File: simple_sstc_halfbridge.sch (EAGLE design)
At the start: 31 parts, among them IC1 IR2153D, J1 DCJ0202, Q1 IRFP240, Q2 IRFP240, Q3 IRLZ44Z

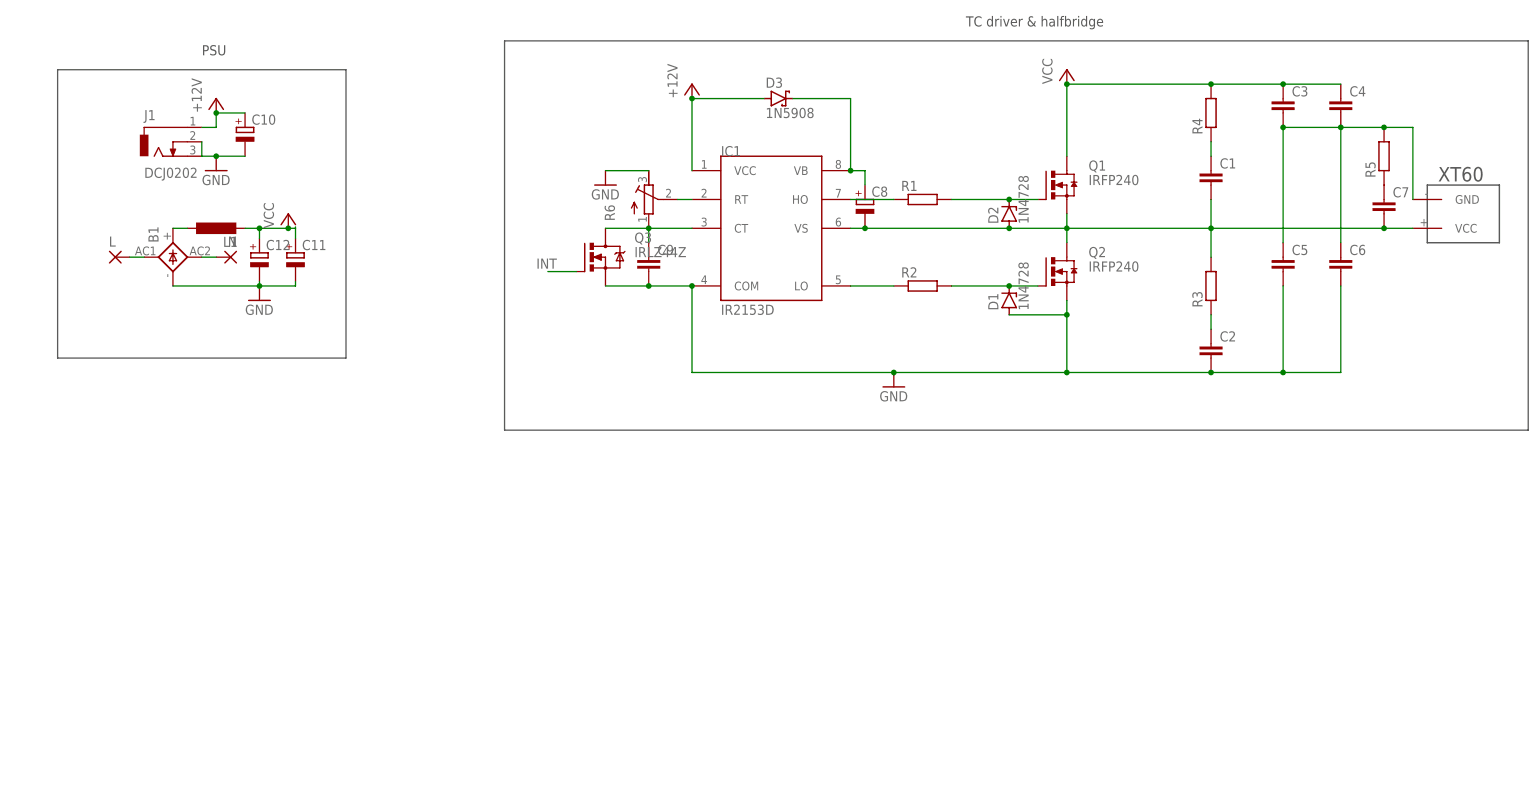
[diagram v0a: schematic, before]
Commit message: Finished driver schematic
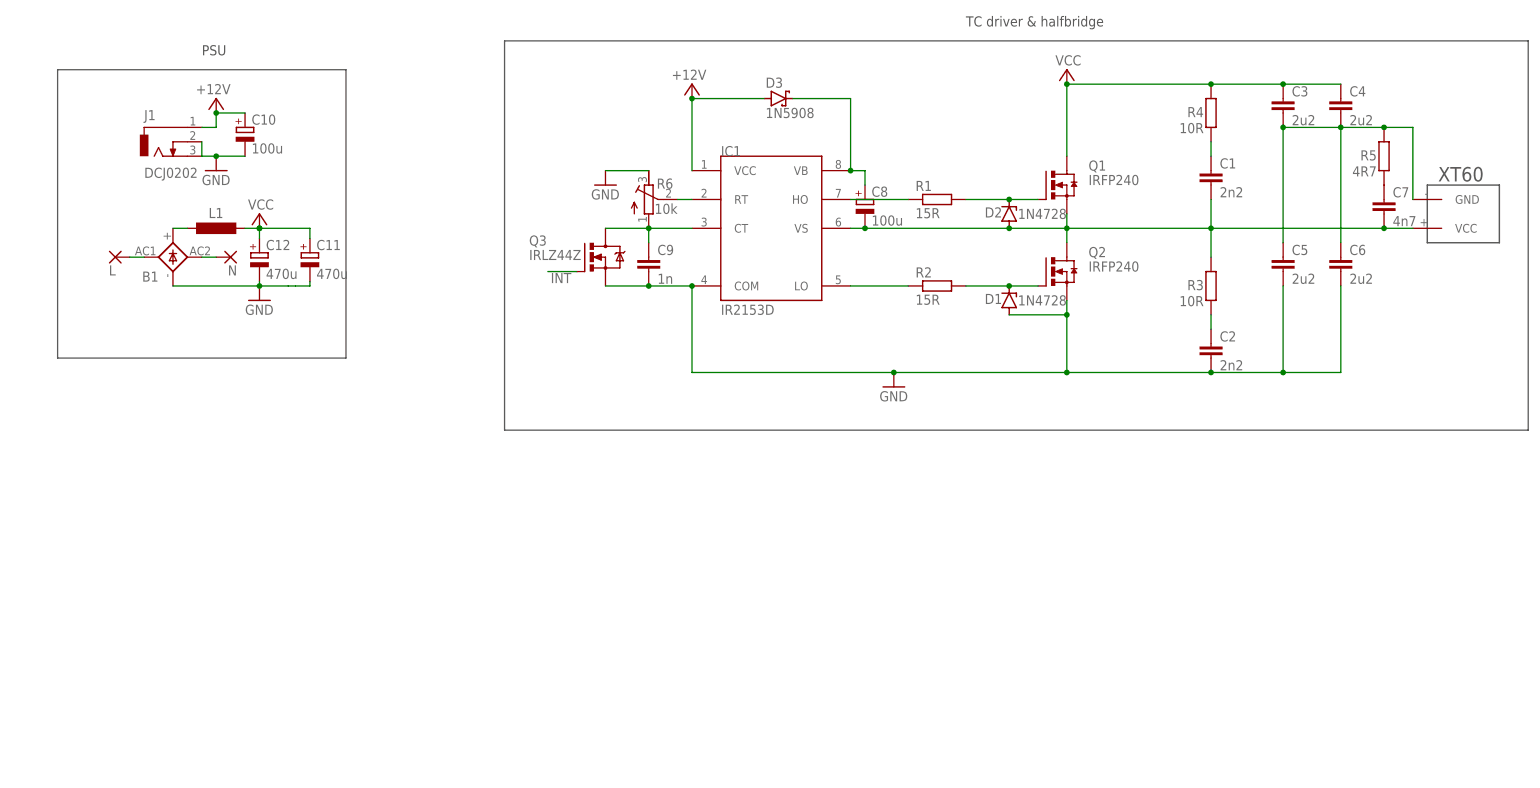
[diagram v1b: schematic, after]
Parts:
- C1, C2: value (none) -> 2n2
- C10, C8: value (none) -> 100u
- C11, C12: value (none) -> 470u
- C3, C4, C5, C6: value (none) -> 2u2
- C7: value (none) -> 4n7
- C9: value (none) -> 1n
- R1, R2: value (none) -> 15R
- R3, R4: value (none) -> 10R
- R5: value (none) -> 4R7
- R6: value (none) -> 10k
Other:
- moved on the sheet: C11, R1, R2

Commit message: Added interrupter
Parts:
- added C13: 10n, rcl:C-EU025-025X050
- added C14: 100n, rcl:C-EU025-025X050
- added IC2: NE555, st-microelectronics:NE555
- added R7: 15k, rcl:R-EU_VMTA55
- added R8: 100k, rcl:R-TRIMM3339P
- added SV1: (no value), con-lstb:MA03-1
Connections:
- new net N$10: IC2.DIS, R7.1, R8.E
- new net N$14: C13.1, IC2.TRE, IC2.TRI, R8.S
- new net N$17: C14.1, IC2.CON
- new net N$19: IC2.OUT, SV1.1
- net GND: now also C13.2, C14.2, IC2.GND, R8.A, SV1.3
- net INT: now also SV1.2
- net VCC: now also IC2./RES, IC2.VCC+, R7.2
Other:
- note added: "Interrupter"
- note added: "Jumper"
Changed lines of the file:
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@@
 <part name="P+3" library="supply1" library_urn="urn:adsk.eagle:library:371" deviceset="VCC" device=""/>
 <part name="P+4" library="supply1" library_urn="urn:adsk.eagle:library:371" deviceset="VCC" device=""/>
+<part name="IC2" library="st-microelectronics" library_urn="urn:adsk.eagle:library:368" deviceset="NE555" device="" package3d_urn="urn:adsk.eagle:package:26829/1"/>
+<part name="C13" library="rcl" library_urn="urn:adsk.eagle:library:334" deviceset="C-EU" device="025-025X050" package3d_urn="urn:adsk.eagle:package:23629/2" value="10n"/>
+<part name="C14" library="rcl" library_urn="urn:adsk.eagle:library:334" deviceset="C-EU" device="025-025X050" package3d_urn="urn:adsk.eagle:package:23629/2" value="100n"/>
+<part name="R7" library="rcl" library_urn="urn:adsk.eagle:library:334" deviceset="R-EU_" device="VMTA55" package3d_urn="urn:adsk.eagle:package:26121/2" value="15k"/>
+<part name="R8" library="rcl" library_urn="urn:adsk.eagle:library:334" deviceset="R-TRIMM" device="3339P" package3d_urn="urn:adsk.eagle:package:23757/1" value="100k"/>
+<part name="P+5" library="supply1" library_urn="urn:adsk.eagle:library:371" deviceset="VCC" device="" value="+12V"/>
+<part name="P+6" library="supply1" library_urn="urn:adsk.eagle:library:371" deviceset="VCC" device="" value="+12V"/>
+<part name="GND5" library="supply1" library_urn="urn:adsk.eagle:library:371" deviceset="GND" device=""/>
+<part name="GND6" library="supply1" library_urn="urn:adsk.eagle:library:371" deviceset="GND" device=""/>
+<part name="SV1" library="con-lstb" library_urn="urn:adsk.eagle:library:162" deviceset="MA03-1" device="" package3d_urn="urn:adsk.eagle:package:8339/1"/>
+<part name="GND7" library="supply1" library_urn="urn:adsk.eagle:library:371" deviceset="GND" device=""/>
+<part name="GND8" library="supply1" library_urn="urn:adsk.eagle:library:371" deviceset="GND" device=""/>
 </parts>
 <sheets>
 <sheet>
 <plain>
-<wire x1="12.7" y1="63.5" x2="63.5" y2="63.5" width="0.1524" layer="97"/>
-<wire x1="63.5" y1="63.5" x2="63.5" y2="12.7" width="0.1524" layer="97"/>
-<wire x1="63.5" y1="12.7" x2="12.7" y2="12.7" width="0.1524" layer="97"/>
-<wire x1="12.7" y1="12.7" x2="12.7" y2="63.5" width="0.1524" layer="97"/>
+<wire x1="12.7" y1="63.5" x2="71.12" y2="63.5" width="0.1524" layer="97"/>
+<wire x1="71.12" y1="63.5" x2="71.12" y2="2.54" width="0.1524" layer="97"/>
+<wire x1="71.12" y1="2.54" x2="12.7" y2="2.54" width="0.1524" layer="97"/>
+<wire x1="12.7" y1="2.54" x2="12.7" y2="63.5" width="0.1524" layer="97"/>
 <wire x1="271.78" y1="68.58" x2="91.44" y2="68.58" width="0.1524" layer="97"/>
 <wire x1="91.44" y1="68.58" x2="91.44" y2="0" width="0.1524" layer="97"/>
@@
 <text x="38.1" y="66.04" size="1.778" layer="97">PSU</text>
 <text x="172.72" y="71.12" size="1.778" layer="97">TC driver &amp; halfbridge</text>
+<wire x1="5.08" y1="-5.08" x2="81.28" y2="-5.08" width="0.1524" layer="97"/>
+<wire x1="81.28" y1="-5.08" x2="81.28" y2="-60.96" width="0.1524" layer="97"/>
+<wire x1="81.28" y1="-60.96" x2="5.08" y2="-60.96" width="0.1524" layer="97"/>
+<wire x1="5.08" y1="-60.96" x2="5.08" y2="-5.08" width="0.1524" layer="97"/>
+<text x="35.56" y="-2.54" size="1.778" layer="97">Interrupter</text>
+<text x="71.12" y="-20.32" size="1.778" layer="97">Jumper</text>
 </plain>
 <instances>
@@
 <instance part="P+4" gate="VCC" x="190.5" y="63.5" smashed="yes">
 <attribute name="VALUE" x="193.04" y="66.04" size="1.778" layer="96" rot="R180"/>
+</instance>
+<instance part="IC2" gate="G$1" x="33.02" y="-25.4" smashed="yes">
+<attribute name="NAME" x="25.4" y="-13.97" size="1.778" layer="95"/>
+<attribute name="VALUE" x="25.4" y="-38.1" size="1.778" layer="96"/>
+</instance>
+<instance part="C13" gate="G$1" x="20.32" y="-43.18" smashed="yes">
+<attribute name="NAME" x="21.844" y="-42.799" size="1.778" layer="95"/>
+<attribute name="VALUE" x="21.844" y="-47.879" size="1.778" layer="96"/>
+</instance>
+<instance part="C14" gate="G$1" x="48.26" y="-33.02" smashed="yes">
+<attribute name="NAME" x="49.784" y="-32.639" size="1.778" layer="95"/>
+<attribute name="VALUE" x="49.784" y="-37.719" size="1.778" layer="96"/>
+</instance>
+<instance part="R7" gate="G$1" x="15.24" y="-20.32" smashed="yes" rot="R90">
+<attribute name="NAME" x="13.97" y="-19.2786" size="1.778" layer="95" rot="R180"/>
+<attribute name="VALUE" x="13.97" y="-22.098" size="1.778" layer="96" rot="R180"/>
+</instance>
+<instance part="R8" gate="G$1" x="15.24" y="-33.02" smashed="yes">
+<attribute name="NAME" x="11.43" y="-31.369" size="1.778" layer="95" rot="R180"/>
+<attribute name="VALUE" x="11.43" y="-34.29" size="1.778" layer="96" rot="R180"/>
+</instance>
+<instance part="P+5" gate="VCC" x="15.24" y="-10.16" smashed="yes">
+<attribute name="VALUE" x="17.78" y="-7.62" size="1.778" layer="96" rot="R180"/>
+</instance>
+<instance part="P+6" gate="VCC" x="43.18" y="-12.7" smashed="yes">
+<attribute name="VALUE" x="45.72" y="-10.16" size="1.778" layer="96" rot="R180"/>
+</instance>
+<instance part="GND5" gate="1" x="48.26" y="-43.18" smashed="yes">
+<attribute name="VALUE" x="45.72" y="-45.72" size="1.778" layer="96"/>
+</instance>
+<instance part="GND6" gate="1" x="20.32" y="-53.34" smashed="yes">
+<attribute name="VALUE" x="17.78" y="-55.88" size="1.778" layer="96"/>
+</instance>
+<instance part="SV1" gate="G$1" x="76.2" y="-27.94" smashed="yes" rot="R180">
+<attribute name="VALUE" x="77.47" y="-20.32" size="1.778" layer="96" rot="R180"/>
+<attribute name="NAME" x="77.47" y="-33.782" size="1.778" layer="95" rot="R180"/>
+</instance>
+<instance part="GND7" gate="1" x="66.04" y="-35.56" smashed="yes">
+<attribute name="VALUE" x="63.5" y="-38.1" size="1.778" layer="96"/>
+</instance>
+<instance part="GND8" gate="1" x="15.24" y="-43.18" smashed="yes">
+<attribute name="VALUE" x="12.7" y="-45.72" size="1.778" layer="96"/>
 </instance>
 </instances>
@@
 <wire x1="190.5" y1="60.96" x2="190.5" y2="48.26" width="0.1524" layer="91"/>
 <junction x="190.5" y="60.96"/>
+</segment>
+<segment>
+<pinref part="P+5" gate="VCC" pin="VCC"/>
+<pinref part="R7" gate="G$1" pin="2"/>
+<wire x1="15.24" y1="-12.7" x2="15.24" y2="-15.24" width="0.1524" layer="91"/>
+</segment>
+<segment>
+<pinref part="IC2" gate="G$1" pin="VCC+"/>
+<pinref part="IC2" gate="G$1" pin="/RES"/>
+<wire x1="43.18" y1="-15.24" x2="43.18" y2="-20.32" width="0.1524" layer="91"/>
+<pinref part="P+6" gate="VCC" pin="VCC"/>
+<wire x1="43.18" y1="-15.24" x2="43.18" y2="-17.78" width="0.1524" layer="91"/>
 </segment>
 </net>
@@
 <wire x1="57.15" y1="25.4" x2="54.61" y2="25.4" width="0.1524" layer="91"/>
 </segment>
+<segment>
+<pinref part="C13" gate="G$1" pin="2"/>
+<pinref part="GND6" gate="1" pin="GND"/>
+<wire x1="20.32" y1="-48.26" x2="20.32" y2="-50.8" width="0.1524" layer="91"/>
+</segment>
+<segment>
+<pinref part="IC2" gate="G$1" pin="GND"/>
+<wire x1="43.18" y1="-33.02" x2="43.18" y2="-40.64" width="0.1524" layer="91"/>
+<pinref part="GND5" gate="1" pin="GND"/>
+<wire x1="43.18" y1="-40.64" x2="48.26" y2="-40.64" width="0.1524" layer="91"/>
+<pinref part="C14" gate="G$1" pin="2"/>
+<wire x1="48.26" y1="-38.1" x2="48.26" y2="-40.64" width="0.1524" layer="91"/>
+<junction x="48.26" y="-40.64"/>
+</segment>
+<segment>
+<pinref part="SV1" gate="G$1" pin="3"/>
+<wire x1="68.58" y1="-30.48" x2="66.04" y2="-30.48" width="0.1524" layer="91"/>
+<pinref part="GND7" gate="1" pin="GND"/>
+<wire x1="66.04" y1="-30.48" x2="66.04" y2="-33.02" width="0.1524" layer="91"/>
+</segment>
+<segment>
+<pinref part="R8" gate="G$1" pin="A"/>
+<pinref part="GND8" gate="1" pin="GND"/>
+<wire x1="15.24" y1="-38.1" x2="15.24" y2="-40.64" width="0.1524" layer="91"/>
+</segment>
 </net>
 <net name="N$5" class="0">
@@
 <label x="99.568" y="25.908" size="1.778" layer="95"/>
 </segment>
+<segment>
+<pinref part="SV1" gate="G$1" pin="2"/>
+<wire x1="68.58" y1="-27.94" x2="60.96" y2="-27.94" width="0.1524" layer="91"/>
+<label x="58.42" y="-30.48" size="1.778" layer="95"/>
+</segment>
 </net>
 <net name="N$12" class="0">
@@
 </segment>
 </net>
+<net name="N$10" class="0">
+<segment>
+<pinref part="IC2" gate="G$1" pin="DIS"/>
+<pinref part="R7" gate="G$1" pin="1"/>
+<wire x1="22.86" y1="-25.4" x2="15.24" y2="-25.4" width="0.1524" layer="91"/>
+<pinref part="R8" gate="G$1" pin="E"/>
+<wire x1="15.24" y1="-25.4" x2="15.24" y2="-27.94" width="0.1524" layer="91"/>
+<junction x="15.24" y="-25.4"/>
+</segment>
+</net>
+<net name="N$14" class="0">
+<segment>
+<pinref part="R8" gate="G$1" pin="S"/>
+<pinref part="IC2" gate="G$1" pin="TRI"/>
+<wire x1="20.32" y1="-33.02" x2="22.86" y2="-33.02" width="0.1524" layer="91"/>
+<pinref part="IC2" gate="G$1" pin="TRE"/>
+<wire x1="22.86" y1="-17.78" x2="20.32" y2="-17.78" width="0.1524" layer="91"/>
+<wire x1="20.32" y1="-17.78" x2="20.32" y2="-33.02" width="0.1524" layer="91"/>
+<junction x="20.32" y="-33.02"/>
+<pinref part="C13" gate="G$1" pin="1"/>
+<wire x1="20.32" y1="-33.02" x2="20.32" y2="-40.64" width="0.1524" layer="91"/>
+</segment>
+</net>
+<net name="N$17" class="0">
+<segment>
+<pinref part="IC2" gate="G$1" pin="CON"/>
+<pinref part="C14" gate="G$1" pin="1"/>
+<wire x1="43.18" y1="-30.48" x2="48.26" y2="-30.48" width="0.1524" layer="91"/>
+</segment>
+</net>
+<net name="N$19" class="0">
+<segment>
+<pinref part="SV1" gate="G$1" pin="1"/>
+<pinref part="IC2" gate="G$1" pin="OUT"/>
+<wire x1="68.58" y1="-25.4" x2="43.18" y2="-25.4" width="0.1524" layer="91"/>
+</segment>
+</net>

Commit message: Started making pcb
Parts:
- L1: device rcl:L-EUTJ7-U2 -> rcl:L-EUTJ4-U2
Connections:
- new net +12V: C10.+, D3.A, IC1.VCC, IC2./RES, IC2.VCC+, J1.1, R7.2
- net VCC: no longer C10.+, D3.A, IC1.VCC, IC2./RES, IC2.VCC+, J1.1, R7.2
